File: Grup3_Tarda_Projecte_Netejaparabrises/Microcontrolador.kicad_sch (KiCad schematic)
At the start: 21 parts, among them IC1 PIC18F258-I_SO, J2 BOTONERA, J3 PROGRAMMING CON, J5 DE9_Plug_MountingHoles, J5 JP1, J6 DE9_Plug_MountingHoles, SW1 SW_Push, SW1 SW_SPST, SW2 SW_SP3T, U1 TCAN1042DRQ1, Y1 ABLS2-8.000MHZ-D4Y-T

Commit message: canvis reles
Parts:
- SW1: footprint Library:AS11CH -> Projecte:AS11CH
- SW2: footprint SW_NR01103ANG13-1C:SW_NR01103ANG13-1C -> Projecte:SW_NR01103ANG13-1C
- Y1: footprint XTAL_ABLS2-8:XTAL_ABLS2-8.000MHZ-D4Y-T -> Projecte:XTAL_ABLS2-8.000MHZ-D4Y-T
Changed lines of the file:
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@@
       (effects (font (size 1.27 1.27)))
     )
-    (property "Footprint" "Library:AS11CH" (at 22.098 161.544 0)
+    (property "Footprint" "Projecte:AS11CH" (at 22.098 161.544 0)
       (effects (font (size 1.27 1.27)) hide)
     )
@@
       (effects (font (size 0.8 0.8)))
     )
-    (property "Footprint" "XTAL_ABLS2-8:XTAL_ABLS2-8.000MHZ-D4Y-T" (at 91.44 128.524 0)
+    (property "Footprint" "Projecte:XTAL_ABLS2-8.000MHZ-D4Y-T" (at 91.44 128.524 0)
       (effects (font (size 1.27 1.27)) (justify bottom) hide)
     )
@@
       (effects (font (size 1.27 1.27)))
     )
-    (property "Footprint" "SW_NR01103ANG13-1C:SW_NR01103ANG13-1C" (at 6.731 128.905 0)
-      (effects (font (size 1.27 1.27)) hide)
-    )
+    (property "Footprint" "Projecte:SW_NR01103ANG13-1C" (at 6.731 128.905 0)
+      (effects (font (size 1.27 1.27)) hide)
+    )

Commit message: Layout 3
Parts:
- SW1: footprint Projecte:AS11CH -> Library:AS11CH
- SW2: footprint Projecte:SW_NR01103ANG13-1C -> SW_NR01103ANG13-1C:SW_NR01103ANG13-1C
- Y1: footprint Projecte:XTAL_ABLS2-8.000MHZ-D4Y-T -> XTAL_ABLS2-8:XTAL_ABLS2-8.000MHZ-D4Y-T
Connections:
- net EnableM1: now also IC1.12 (RC1/T1OSI); no longer IC1.13 (RC2/CCP1)
- net EnableM2: now also IC1.13 (RC2/CCP1); no longer IC1.12 (RC1/T1OSI)
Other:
- moved on the sheet: C2, J3, J5, J6, R6, Rterm1, SW1, U1

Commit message: routing v1 sense acabar
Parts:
- removed SW1: SW_SPST, Library:AS11CH, symbol Switch:SW_SPST
- removed SW2: SW_SP3T, SW_NR01103ANG13-1C:SW_NR01103ANG13-1C, symbol Switch:SW_SP3T
- C1, C2: footprint Capacitor_SMD:C_0805_2012Metric -> Capacitor_THT:C_Disc_D3.0mm_W1.6mm_P2.50mm
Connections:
- net CANH renamed CAN-
- net CANL renamed CAN+
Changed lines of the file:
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@@
   (junction (at 44.704 161.544) (diameter 0) (color 0 0 0 0)
   )
-  (junction (at 31.75 161.544) (diameter 0) (color 0 0 0 0)
-  )
   (junction (at 91.948 138.684) (diameter 0) (color 0 0 0 0)
   )
-  (junction (at 40.894 123.444) (diameter 0) (color 0 0 0 0)
-  )
   (junction (at 47.498 114.554) (diameter 0) (color 0 0 0 0)
   )
@@
   )
   (junction (at 82.804 128.524) (diameter 0) (color 0 0 0 0)
-  )
-  (junction (at 33.274 135.89) (diameter 0) (color 0 0 0 0)
-  )
-  (junction (at 37.592 104.394) (diameter 0) (color 0 0 0 0)
   )
   (no_connect (at 173.482 114.554))
@@
     (stroke (width 0) (type default))
   )
-  (wire (pts (xy 37.592 104.394) (xy 37.592 130.81))
-    (stroke (width 0) (type default))
-  )
   (wire (pts (xy 21.082 112.014) (xy 35.814 112.014))
     (stroke (width 0) (type default))
@@
     (stroke (width 0) (type default))
   )
-  (wire (pts (xy 40.894 133.35) (xy 27.686 133.35))
-    (stroke (width 0) (type default))
-  )
   (wire (pts (xy 100.33 104.394) (xy 115.062 104.394))
     (stroke (width 0) (type default))
@@
     (stroke (width 0) (type default))
   )
-  (wire (pts (xy 37.592 130.81) (xy 27.686 130.81))
-    (stroke (width 0) (type default))
-  )
   (wire (pts (xy 64.516 94.234) (xy 115.062 94.234))
     (stroke (width 0) (type default))
@@
     (stroke (width 0) (type default))
   )
-  (wire (pts (xy 37.592 104.394) (xy 44.704 104.394))
+  (wire (pts (xy 21.082 104.394) (xy 44.704 104.394))
     (stroke (width 0) (type default))
   )
@@
     (stroke (width 0) (type default))
   )
-  (wire (pts (xy 40.894 123.444) (xy 40.894 133.35))
-    (stroke (width 0) (type default))
-  )
   (wire (pts (xy 181.991 109.474) (xy 173.482 109.474))
     (stroke (width 0) (type default))
   )
-  (wire (pts (xy 27.686 135.89) (xy 33.274 135.89))
-    (stroke (width 0) (type default))
-  )
   (wire (pts (xy 37.084 56.896) (xy 37.084 59.436))
     (stroke (width 0) (type default))
@@
     (stroke (width 0) (type default))
   )
-  (wire (pts (xy 15.748 133.35) (xy 17.526 133.35))
-    (stroke (width 0) (type default))
-  )
   (wire (pts (xy 183.134 123.063) (xy 212.09 123.063))
     (stroke (width 0) (type default))
@@
     (stroke (width 0) (type default))
   )
-  (wire (pts (xy 33.274 135.89) (xy 33.274 109.474))
+  (wire (pts (xy 33.274 109.474) (xy 33.274 143.764))
     (stroke (width 0) (type default))
   )
@@
     (stroke (width 0) (type default))
   )
-  (wire (pts (xy 33.274 143.764) (xy 33.274 135.89))
-    (stroke (width 0) (type default))
-  )
   (wire (pts (xy 218.694 128.778) (xy 221.996 128.778))
     (stroke (width 0) (type default))
   )
-  (wire (pts (xy 14.986 161.544) (xy 17.018 161.544))
-    (stroke (width 0) (type default))
-  )
   (wire (pts (xy 58.166 123.444) (xy 58.166 89.154))
     (stroke (width 0) (type default))
@@
     (stroke (width 0) (type default))
   )
-  (wire (pts (xy 27.178 161.544) (xy 31.75 161.544))
-    (stroke (width 0) (type default))
-  )
   (wire (pts (xy 100.33 104.394) (xy 100.33 128.524))
     (stroke (width 0) (type default))
@@
   )
   (wire (pts (xy 34.544 56.896) (xy 34.544 68.326))
-    (stroke (width 0) (type default))
-  )
-  (wire (pts (xy 21.082 104.394) (xy 37.592 104.394))
     (stroke (width 0) (type default))
   )
@@
     (effects (font (size 5 5) bold) (justify left bottom))
   )
-  (label "CANL" (at 235.712 96.774 0) (fields_autoplaced)
+  (label "CAN+" (at 235.712 96.774 0) (fields_autoplaced)
     (effects (font (size 1.27 1.27)) (justify left bottom))
   )
@@
     (effects (font (size 1.27 1.27)) (justify left bottom))
   )
-  (label "CANH" (at 236.728 104.394 0) (fields_autoplaced)
+  (label "CAN-" (at 236.728 104.394 0) (fields_autoplaced)
     (effects (font (size 1.27 1.27)) (justify left bottom))
   )
@@
       (effects (font (size 1.27 1.27)) (justify left))
     )
-    (property "Footprint" "Capacitor_SMD:C_0805_2012Metric" (at 202.6412 114.427 0)
+    (property "Footprint" "Capacitor_THT:C_Disc_D3.0mm_W1.6mm_P2.50mm" (at 202.6412 114.427 0)
       (effects (font (size 1.27 1.27)) hide)
     )
@@
       (effects (font (size 1.27 1.27)) (justify left))
     )
-    (property "Footprint" "Capacitor_SMD:C_0805_2012Metric" (at 101.2952 138.684 0)
+    (property "Footprint" "Capacitor_THT:C_Disc_D3.0mm_W1.6mm_P2.50mm" (at 101.2952 138.684 0)
       (effects (font (size 1.27 1.27)) hide)
     )
@@
       (effects (font (size 1.27 1.27)) (justify left))
     )
-    (property "Footprint" "Capacitor_SMD:C_0805_2012Metric" (at 83.7692 138.684 0)
+    (property "Footprint" "Capacitor_THT:C_Disc_D3.0mm_W1.6mm_P2.50mm" (at 83.7692 138.684 0)
       (effects (font (size 1.27 1.27)) hide)
     )
@@
         (path "/f9f603a9-b774-48a7-94d1-4c8d3d65a3f8"
           (reference "C1") (unit 1)
-        )
-      )
-    )
-  )
-  (symbol (lib_id "power:GND") (at 15.748 133.35 0) (unit 1)
-    (in_bom yes) (on_board yes) (dnp no)
-    (property "Reference" "#PWR05" (at 15.748 139.7 0)
-      (effects (font (size 1.27 1.27)) hide)
-    )
-    (property "Value" "GND" (at 13.97 137.414 0)
-      (effects (font (size 1.27 1.27)) (justify left))
-    )
-    (property "Footprint" "" (at 15.748 133.35 0)
-      (effects (font (size 1.27 1.27)) hide)
-    )
-    (property "Datasheet" "" (at 15.748 133.35 0)
-      (effects (font (size 1.27 1.27)) hide)
-    )
-    (pin "1")
-    (instances
-      (project "Grup3_Tarda_Projecte_Netejaparabrises"
-        (path "/7ae78f34-680b-4fd9-8391-ce3e1c73c4b5/41ec4c6b-5222-4808-bf2f-f72f20229182"
-          (reference "#PWR05") (unit 1)
         )
       )
@@
     )
   )
-  (symbol (lib_id "Switch:SW_SPST") (at 22.098 161.544 0) (unit 1)
-    (in_bom yes) (on_board yes) (dnp no) (fields_autoplaced)
-    (property "Reference" "SW1" (at 22.098 155.702 0)
-      (effects (font (size 1.27 1.27)))
-    )
-    (property "Value" "SW_SPST" (at 22.098 158.242 0)
-      (effects (font (size 1.27 1.27)))
-    )
-    (property "Footprint" "Library:AS11CH" (at 22.098 161.544 0)
-      (effects (font (size 1.27 1.27)) hide)
-    )
-    (property "Datasheet" "~" (at 22.098 161.544 0)
-      (effects (font (size 1.27 1.27)) hide)
-    )
-    (pin "1")
-    (pin "2")
-    (instances
-      (project "Grup3_Tarda_Projecte_Netejaparabrises"
-        (path "/7ae78f34-680b-4fd9-8391-ce3e1c73c4b5/41ec4c6b-5222-4808-bf2f-f72f20229182"
-          (reference "SW1") (unit 1)
-        )
-      )
-    )
-  )
   (symbol (lib_id "Switch:SW_Push") (at 96.774 69.85 0) (unit 1)
     (in_bom yes) (on_board yes) (dnp no)
@@
       (effects (font (size 1.27 1.27)) (justify left))
     )
-    (property "Footprint" "Capacitor_SMD:C_0805_2012Metric" (at 193.4972 114.427 0)
+    (property "Footprint" "Capacitor_THT:C_Disc_D3.0mm_W1.6mm_P2.50mm" (at 193.4972 114.427 0)
       (effects (font (size 1.27 1.27)) hide)
     )
@@
         (path "/7ae78f34-680b-4fd9-8391-ce3e1c73c4b5/41ec4c6b-5222-4808-bf2f-f72f20229182"
           (reference "#PWR013") (unit 1)
-        )
-      )
-    )
-  )
-  (symbol (lib_id "Switch:SW_SP3T") (at 22.606 133.35 0) (unit 1)
-    (in_bom yes) (on_board yes) (dnp no) (fields_autoplaced)
-    (property "Reference" "SW2" (at 22.606 126.746 0)
-      (effects (font (size 1.27 1.27)))
-    )
-    (property "Value" "SW_SP3T" (at 22.606 129.286 0)
-      (effects (font (size 1.27 1.27)))
-    )
-    (property "Footprint" "SW_NR01103ANG13-1C:SW_NR01103ANG13-1C" (at 6.731 128.905 0)
-      (effects (font (size 1.27 1.27)) hide)
-    )
-    (property "Datasheet" "~" (at 6.731 128.905 0)
-      (effects (font (size 1.27 1.27)) hide)
-    )
-    (pin "1")
-    (pin "2")
-    (pin "3")
-    (pin "4")
-    (instances
-      (project "Grup3_Tarda_Projecte_Netejaparabrises"
-        (path "/7ae78f34-680b-4fd9-8391-ce3e1c73c4b5/41ec4c6b-5222-4808-bf2f-f72f20229182"
-          (reference "SW2") (unit 1)
         )
       )
@@
         )
       )
-    )
-  )
-  (symbol (lib_id "power:GND") (at 14.986 161.544 0) (unit 1)
-    (in_bom yes) (on_board yes) (dnp no)
-    (property "Reference" "#PWR045" (at 14.986 167.894 0)
-      (effects (font (size 1.27 1.27)) hide)
-    )
-    (property "Value" "GND" (at 13.208 165.608 0)
-      (effects (font (size 1.27 1.27)) (justify left))
-    )
-    (property "Footprint" "" (at 14.986 161.544 0)
-      (effects (font (size 1.27 1.27)) hide)
-    )
-    (property "Datasheet" "" (at 14.986 161.544 0)
-      (effects (font (size 1.27 1.27)) hide)
-    )
-    (pin "1")
-    (instances
-      (project "Grup3_Tarda_Projecte_Netejaparabrises"
-        (path "/7ae78f34-680b-4fd9-8391-ce3e1c73c4b5/41ec4c6b-5222-4808-bf2f-f72f20229182"
-          (reference "#PWR045") (unit 1)
-        )
-      )

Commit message: placing rooting
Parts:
- C1, C2: footprint Capacitor_THT:C_Disc_D3.0mm_W1.6mm_P2.50mm -> Capacitor_SMD:C_0805_2012Metric_Pad1.18x1.45mm_HandSolder
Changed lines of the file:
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@@
       (effects (font (size 1.27 1.27)) (justify left))
     )
-    (property "Footprint" "Capacitor_THT:C_Disc_D3.0mm_W1.6mm_P2.50mm" (at 202.6412 114.427 0)
+    (property "Footprint" "Capacitor_SMD:C_0805_2012Metric_Pad1.18x1.45mm_HandSolder" (at 202.6412 114.427 0)
       (effects (font (size 1.27 1.27)) hide)
     )
@@
       (effects (font (size 1.27 1.27)) (justify left))
     )
-    (property "Footprint" "Capacitor_THT:C_Disc_D3.0mm_W1.6mm_P2.50mm" (at 101.2952 138.684 0)
+    (property "Footprint" "Capacitor_SMD:C_0805_2012Metric_Pad1.18x1.45mm_HandSolder" (at 101.2952 138.684 0)
       (effects (font (size 1.27 1.27)) hide)
     )
@@
       (effects (font (size 1.27 1.27)) (justify left))
     )
-    (property "Footprint" "Capacitor_THT:C_Disc_D3.0mm_W1.6mm_P2.50mm" (at 83.7692 138.684 0)
+    (property "Footprint" "Capacitor_SMD:C_0805_2012Metric_Pad1.18x1.45mm_HandSolder" (at 83.7692 138.684 0)
       (effects (font (size 1.27 1.27)) hide)
     )
@@
       (effects (font (size 1.27 1.27)) (justify left))
     )
-    (property "Footprint" "Capacitor_THT:C_Disc_D3.0mm_W1.6mm_P2.50mm" (at 193.4972 114.427 0)
-      (effects (font (size 1.27 1.27)) hide)
-    )
+    (property "Footprint" "Capacitor_SMD:C_0805_2012Metric_Pad1.18x1.45mm_HandSolder" (at 193.4972 114.427 0)
+      (effects (font (size 1.27 1.27)) hide)
+    )

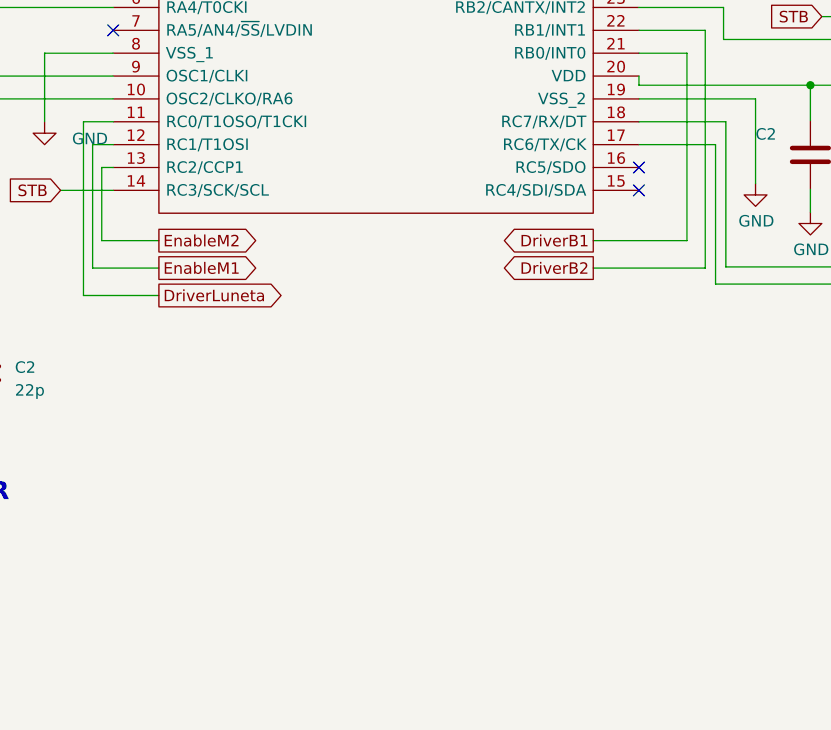
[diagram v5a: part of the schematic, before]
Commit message: redefinicio copper pours, rerouting, final de carrera i teardrops
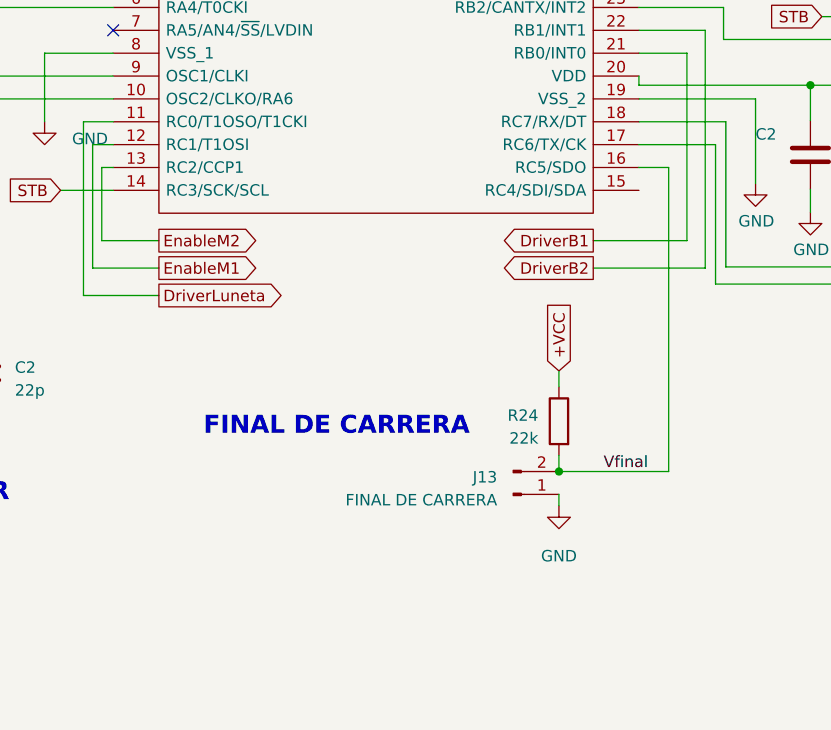
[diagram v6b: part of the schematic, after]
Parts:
- added J13: FINAL DE CARRERA, Connector_PinSocket_1.00mm:PinSocket_1x02_P1.00mm_Vertical, symbol Connector:Conn_01x02_Pin
- added R24: 22k, Resistor_SMD:R_0805_2012Metric_Pad1.20x1.40mm_HandSolder, symbol Device:R
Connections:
- net +VCC: now also R24.1
- net GND: now also J13.1 (Pin_1)
- net Vfinal: now reaches IC1.16 (RC5/SDO)
- net Vfinal: now also J13.2 (Pin_2), R24.2
- no-connect marks 18 -> 16
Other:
- note added: "FINAL DE CARRERA"
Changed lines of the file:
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@@
   (junction (at 201.676 102.87) (diameter 0) (color 0 0 0 0)
   )
+  (junction (at 164.592 145.796) (diameter 0) (color 0 0 0 0)
+  )
   (junction (at 44.704 161.544) (diameter 0) (color 0 0 0 0)
   )
@@
   (junction (at 82.804 128.524) (diameter 0) (color 0 0 0 0)
   )
-  (no_connect (at 173.482 114.554))
   (no_connect (at 244.856 100.33))
   (no_connect (at 244.856 97.79))
@@
   (no_connect (at 221.996 133.858))
   (no_connect (at 229.616 154.178))
+  (no_connect (at 115.062 96.774))
   (no_connect (at 244.856 105.41))
   (no_connect (at 244.856 107.95))
   (no_connect (at 221.996 136.398))
-  (no_connect (at 173.482 112.014))
   (no_connect (at 221.996 141.478))
   (no_connect (at 244.856 87.63))
   (no_connect (at 203.708 100.33))
   (no_connect (at 221.996 146.558))
-  (no_connect (at 115.062 96.774))
+  (wire (pts (xy 164.592 145.796) (xy 176.784 145.796))
+    (stroke (width 0) (type default))
+  )
   (wire (pts (xy 47.498 132.334) (xy 47.498 152.908))
     (stroke (width 0) (type default))
@@
     (stroke (width 0) (type default))
   )
+  (wire (pts (xy 164.592 134.62) (xy 164.592 136.398))
+    (stroke (width 0) (type default))
+  )
   (wire (pts (xy 183.134 106.934) (xy 173.482 106.934))
     (stroke (width 0) (type default))
@@
     (stroke (width 0) (type default))
   )
+  (wire (pts (xy 164.592 144.018) (xy 164.592 145.796))
+    (stroke (width 0) (type default))
+  )
   (wire (pts (xy 183.134 106.934) (xy 183.134 123.063))
     (stroke (width 0) (type default))
@@
     (stroke (width 0) (type default))
   )
+  (wire (pts (xy 164.592 148.336) (xy 164.592 149.606))
+    (stroke (width 0) (type default))
+  )
   (wire (pts (xy 82.804 128.524) (xy 82.804 131.064))
     (stroke (width 0) (type default))
@@
     (stroke (width 0) (type default))
   )
+  (wire (pts (xy 176.784 145.796) (xy 176.784 112.014))
+    (stroke (width 0) (type default))
+  )
   (wire (pts (xy 201.676 83.82) (xy 201.676 102.87))
     (stroke (width 0) (type default))
@@
   )
   (wire (pts (xy 34.544 56.896) (xy 34.544 68.326))
+    (stroke (width 0) (type default))
+  )
+  (wire (pts (xy 176.784 112.014) (xy 173.482 112.014))
     (stroke (width 0) (type default))
   )
@@
     (effects (font (size 3 3) (thickness 0.6) bold) (justify left bottom))
   )
+  (text "FINAL DE CARRERA" (at 154.686 141.986 0)
+    (effects (font (size 2 2) (thickness 0.6) bold) (justify right bottom))
+  )
   (text "BOTONERA" (at 36.576 86.36 0)
     (effects (font (size 2 2) (thickness 1) bold) (justify left bottom))
@@
   (label "Vsw" (at 84.836 69.85 0) (fields_autoplaced)
     (effects (font (size 1.27 1.27)) (justify left bottom))
+  )
+  (label "Vfinal" (at 174.498 145.796 180) (fields_autoplaced)
+    (effects (font (size 1.27 1.27)) (justify right bottom))
   )
   (label "XTAL1" (at 82.804 121.412 90) (fields_autoplaced)
@@
     (property "Intersheetrefs" "${INTERSHEET_REFS}" (at 185.2778 84.074 0)
       (effects (font (size 1.27 1.27)) (justify left) hide)
+    )
+  )
+  (global_label "+VCC" (shape input) (at 164.592 134.62 90) (fields_autoplaced)
+    (effects (font (size 1.27 1.27)) (justify left))
+    (property "Intersheetrefs" "${INTERSHEET_REFS}" (at 164.592 126.5132 90)
+      (effects (font (size 1.27 1.27)) (justify right) hide)
     )
   )
@@
         (path "/7ae78f34-680b-4fd9-8391-ce3e1c73c4b5/41ec4c6b-5222-4808-bf2f-f72f20229182"
           (reference "RBot3") (unit 1)
+        )
+      )
+    )
+  )
+  (symbol (lib_id "Device:R") (at 164.592 140.208 0) (mirror y) (unit 1)
+    (in_bom yes) (on_board yes) (dnp no) (fields_autoplaced)
+    (property "Reference" "R24" (at 162.306 139.573 0)
+      (effects (font (size 1.27 1.27)) (justify left))
+    )
+    (property "Value" "22k" (at 162.306 142.113 0)
+      (effects (font (size 1.27 1.27)) (justify left))
+    )
+    (property "Footprint" "Resistor_SMD:R_0805_2012Metric_Pad1.20x1.40mm_HandSolder" (at 166.37 140.208 90)
+      (effects (font (size 1.27 1.27)) hide)
+    )
+    (property "Datasheet" "~" (at 164.592 140.208 0)
+      (effects (font (size 1.27 1.27)) hide)
+    )
+    (pin "1")
+    (pin "2")
+    (instances
+      (project "Grup3_Tarda_Projecte_Netejaparabrises"
+        (path "/7ae78f34-680b-4fd9-8391-ce3e1c73c4b5/41ec4c6b-5222-4808-bf2f-f72f20229182"
+          (reference "R24") (unit 1)
+        )
+      )
+    )
+  )
+  (symbol (lib_id "Connector:Conn_01x02_Pin") (at 159.512 148.336 0) (mirror x) (unit 1)
+    (in_bom yes) (on_board yes) (dnp no) (fields_autoplaced)
+    (property "Reference" "J13" (at 157.734 146.431 0)
+      (effects (font (size 1.27 1.27)) (justify right))
+    )
+    (property "Value" "FINAL DE CARRERA" (at 157.734 148.971 0)
+      (effects (font (size 1.27 1.27)) (justify right))
+    )
+    (property "Footprint" "Connector_PinSocket_1.00mm:PinSocket_1x02_P1.00mm_Vertical" (at 159.512 148.336 0)
+      (effects (font (size 1.27 1.27)) hide)
+    )
+    (property "Datasheet" "~" (at 159.512 148.336 0)
+      (effects (font (size 1.27 1.27)) hide)
+    )
+    (pin "1")
+    (pin "2")
+    (instances
+      (project "Grup3_Tarda_Projecte_Netejaparabrises"
+        (path "/7ae78f34-680b-4fd9-8391-ce3e1c73c4b5/41ec4c6b-5222-4808-bf2f-f72f20229182"
+          (reference "J13") (unit 1)
         )
       )
@@
         )
       )
+    )
+  )
+  (symbol (lib_id "power:GND") (at 164.592 149.606 0) (mirror y) (unit 1)
+    (in_bom yes) (on_board yes) (dnp no) (fields_autoplaced)
+    (property "Reference" "#PWR05" (at 164.592 155.956 0)
+      (effects (font (size 1.27 1.27)) hide)
+    )
+    (property "Value" "GND" (at 164.592 155.194 0)
+      (effects (font (size 1.27 1.27)))
+    )
+    (property "Footprint" "" (at 164.592 149.606 0)
+      (effects (font (size 1.27 1.27)) hide)
+    )
+    (property "Datasheet" "" (at 164.592 149.606 0)
+      (effects (font (size 1.27 1.27)) hide)
+    )
+    (pin "1")
+    (instances
+      (project "Grup3_Tarda_Projecte_Netejaparabrises"
+        (path "/7ae78f34-680b-4fd9-8391-ce3e1c73c4b5/41ec4c6b-5222-4808-bf2f-f72f20229182"
+          (reference "#PWR05") (unit 1)
+        )
+      )
